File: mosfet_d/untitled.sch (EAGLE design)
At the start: 47 parts

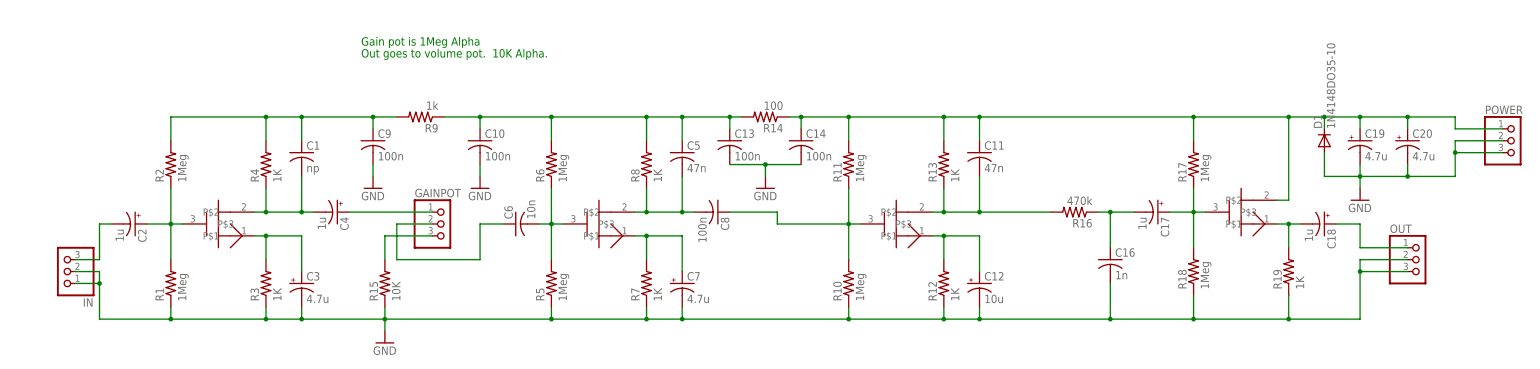
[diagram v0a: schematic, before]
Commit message: fixed pinout of transistors in mosfet d
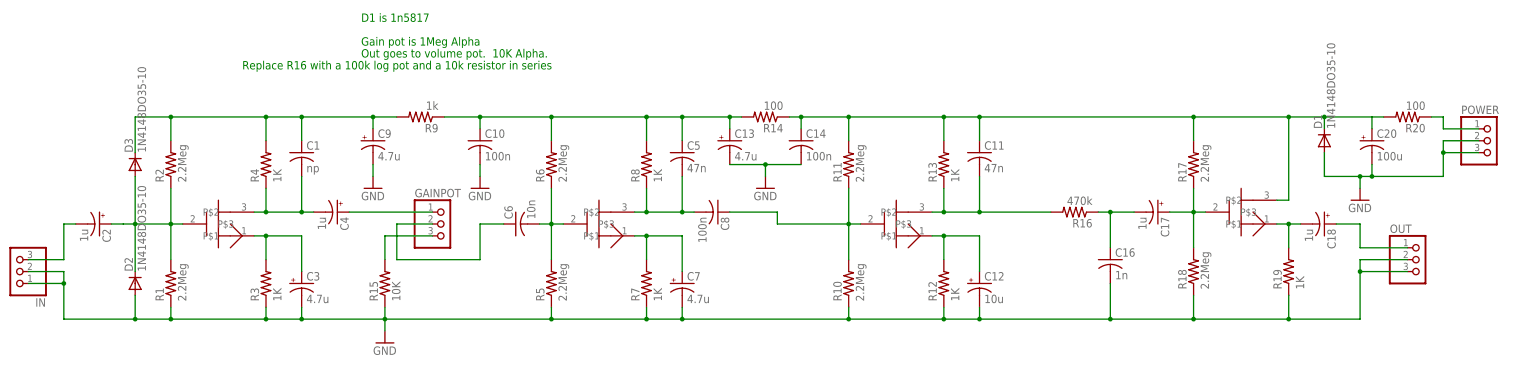
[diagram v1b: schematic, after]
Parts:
- removed C19: 4.7u, dan:CPOL-USE2-5
- added D2, D3: 1N4148DO35-10, dan:1N4148DO35-10
- added R20: 100, dan:R-US_0207/7
- C13, C9: value 100n -> 4.7u; device dan:C-US050-030X075 -> dan:CPOL-USE2-5
- C20: value 4.7u -> 100u
- R1, R10, R11, R17, R18, R2, R5, R6: value 1Meg -> 2.2Meg
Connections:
- new net N$17: C2.+
- new net N$18: POWER.1, R20.1
- net GND: now also C13.-, C9.-, D2.A; no longer C13.2, C19.-, C9.2
- net N$1: now also D2.C, D3.A; no longer C2.+
- net N$13: now also C13.+; no longer C13.1
- net N$20: now also R20.2; no longer C19.+, POWER.1
- net N$3: now also C9.+, D3.C; no longer C9.1
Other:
- note added: "D1 is 1n5817"
- note added: "Replace R16 with a 100k log pot and a 10k resistor in series"
- moved on the sheet: C2, C20, IN, POWER

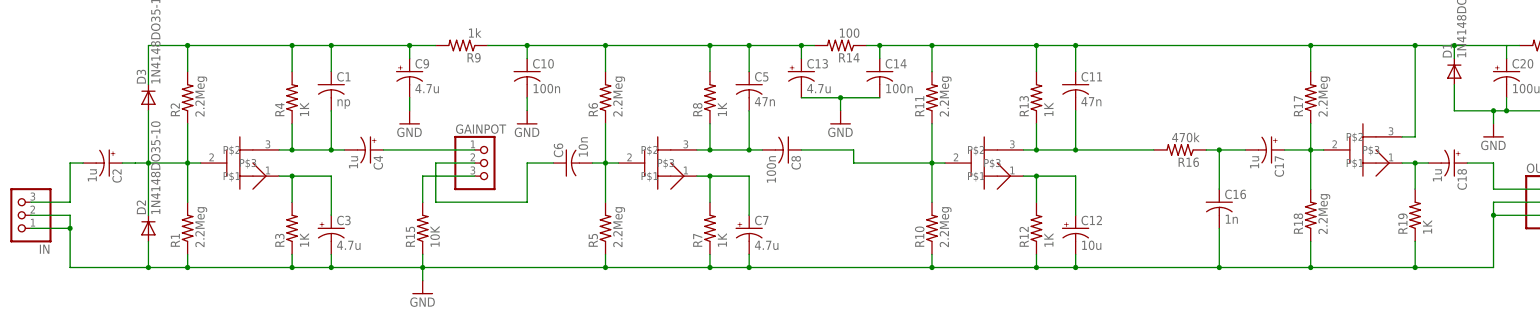
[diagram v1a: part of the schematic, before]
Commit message: fixed component values in mosfet d
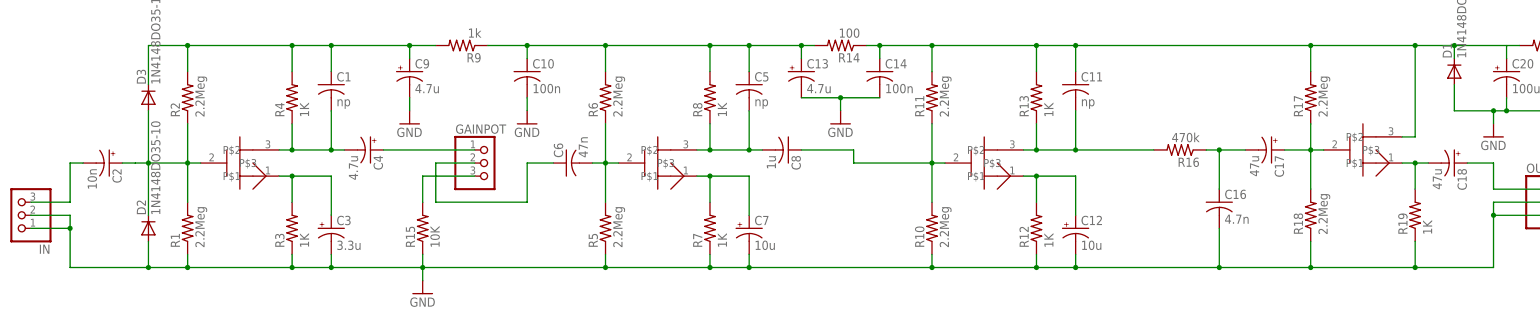
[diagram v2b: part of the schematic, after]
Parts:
- C11, C5: value 47n -> np
- C16: value 1n -> 4.7n
- C17, C18: value 1u -> 47u
- C2: value 1u -> 10n
- C3: value 4.7u -> 3.3u
- C4: value 1u -> 4.7u
- C6: value 10n -> 47n
- C7: value 4.7u -> 10u
- C8: value 100n -> 1u
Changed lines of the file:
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@@
 <part name="R3" library="dan" deviceset="R-US_" device="0207/7" value="1K"/>
 <part name="R4" library="dan" deviceset="R-US_" device="0207/7" value="1K"/>
-<part name="C2" library="dan" deviceset="CPOL-US" device="E2-5" value="1u"/>
-<part name="C3" library="dan" deviceset="CPOL-US" device="E2-5" value="4.7u"/>
+<part name="C2" library="dan" deviceset="CPOL-US" device="E2-5" value="10n"/>
+<part name="C3" library="dan" deviceset="CPOL-US" device="E2-5" value="3.3u"/>
 <part name="GAINPOT" library="dan" deviceset="PINHD-1X3" device=""/>
 <part name="GND1" library="dan" deviceset="GND" device=""/>
-<part name="C4" library="dan" deviceset="CPOL-US" device="E2-5" value="1u"/>
+<part name="C4" library="dan" deviceset="CPOL-US" device="E2-5" value="4.7u"/>
 <part name="U$2" library="dan" deviceset="2N7000_2" device=""/>
-<part name="C5" library="dan" deviceset="C-US" device="050-030X075" value="47n"/>
+<part name="C5" library="dan" deviceset="C-US" device="050-030X075" value="np"/>
 <part name="R5" library="dan" deviceset="R-US_" device="0207/7" value="2.2Meg"/>
 <part name="R6" library="dan" deviceset="R-US_" device="0207/7" value="2.2Meg"/>
 <part name="R7" library="dan" deviceset="R-US_" device="0207/7" value="1K"/>
 <part name="R8" library="dan" deviceset="R-US_" device="0207/7" value="1K"/>
-<part name="C7" library="dan" deviceset="CPOL-US" device="E2-5" value="4.7u"/>
-<part name="C6" library="dan" deviceset="C-US" device="050-030X075" value="10n"/>
-<part name="C8" library="dan" deviceset="C-US" device="050-030X075" value="100n"/>
+<part name="C7" library="dan" deviceset="CPOL-US" device="E2-5" value="10u"/>
+<part name="C6" library="dan" deviceset="C-US" device="050-030X075" value="47n"/>
+<part name="C8" library="dan" deviceset="C-US" device="050-030X075" value="1u"/>
 <part name="R9" library="dan" deviceset="R-US_" device="0207/7" value="1k"/>
 <part name="C10" library="dan" deviceset="C-US" device="050-030X075" value="100n"/>
@@
 <part name="GND3" library="dan" deviceset="GND" device=""/>
 <part name="U$3" library="dan" deviceset="2N7000_2" device=""/>
-<part name="C11" library="dan" deviceset="C-US" device="050-030X075" value="47n"/>
+<part name="C11" library="dan" deviceset="C-US" device="050-030X075" value="np"/>
 <part name="R10" library="dan" deviceset="R-US_" device="0207/7" value="2.2Meg"/>
 <part name="R11" library="dan" deviceset="R-US_" device="0207/7" value="2.2Meg"/>
@@
 <part name="GND4" library="dan" deviceset="GND" device=""/>
 <part name="R16" library="dan" deviceset="R-US_" device="0207/7" value="470k"/>
-<part name="C16" library="dan" deviceset="C-US" device="050-030X075" value="1n"/>
-<part name="C17" library="dan" deviceset="CPOL-US" device="E2-5" value="1u"/>
+<part name="C16" library="dan" deviceset="C-US" device="050-030X075" value="4.7n"/>
+<part name="C17" library="dan" deviceset="CPOL-US" device="E2-5" value="47u"/>
 <part name="R17" library="dan" deviceset="R-US_" device="0207/7" value="2.2Meg"/>
 <part name="R18" library="dan" deviceset="R-US_" device="0207/7" value="2.2Meg"/>
 <part name="U$4" library="dan" deviceset="2N7000_2" device=""/>
 <part name="R19" library="dan" deviceset="R-US_" device="0207/7" value="1K"/>
-<part name="C18" library="dan" deviceset="CPOL-US" device="E2-5" value="1u"/>
+<part name="C18" library="dan" deviceset="CPOL-US" device="E2-5" value="47u"/>
 <part name="OUT" library="dan" deviceset="PINHD-1X3" device=""/>
 <part name="IN" library="dan" deviceset="PINHD-1X3" device=""/>

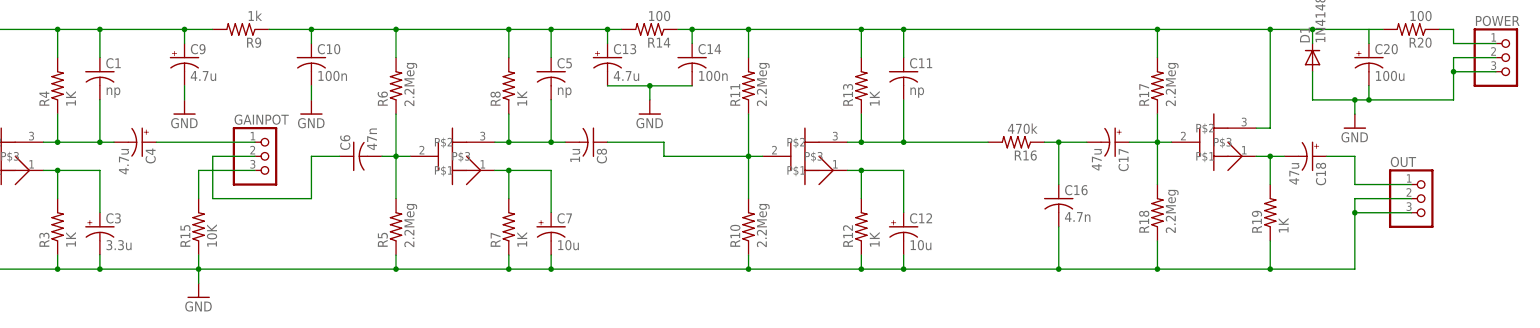
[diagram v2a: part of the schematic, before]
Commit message: added pcb mounted pots to distortion
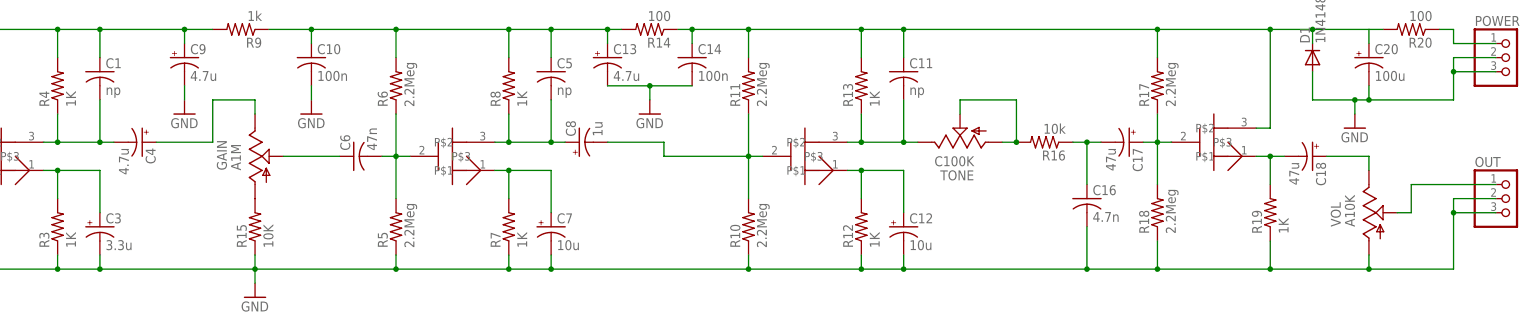
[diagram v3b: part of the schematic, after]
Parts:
- removed GAINPOT: (no value), dan:PINHD-1X3
- added GAIN: A1M, dan:PEDALPOT
- added TONE: C100K, dan:PEDALPOT
- added VOL: A10K, dan:PEDALPOT
- C8: device dan:C-US050-030X075 -> dan:CPOL-USE2-5
- R16: value 470k -> 10k
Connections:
- new net N$21: R16.2, TONE.A, TONE.S
- new net N$25: OUT.1, VOL.S
- net GND: now also VOL.A
- net N$11: now also GAIN.S; no longer GAINPOT.2
- net N$12: now also TONE.E; no longer R16.2
- net N$15: now also C8.-; no longer C8.1
- net N$16: now also GAIN.A; no longer GAINPOT.3
- net N$23: now also VOL.E; no longer OUT.1
- net N$4: now also GAIN.E; no longer GAINPOT.1
- net N$7: now also C8.+; no longer C8.2
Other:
- moved on the sheet: C16, C17, OUT, R15, R16

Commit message: redesigned the distortion pcb
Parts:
- added C15: np, dan:C-US050-030X075
- added C19: 10u, dan:CPOL-USE2-5
- added C21: 1u, dan:CPOL-USE2-5
- added C22: 22n, dan:C-US050-030X075
- added R21, R22: 2.2M, dan:R-US_0207/7
- added R23, R24: 1K, dan:R-US_0207/7
- added R25: 100k, dan:R-US_0207/7
- added R26: 22k, dan:R-US_0207/7
- added R27: 220k, dan:R-US_0207/7
- added U$5: 2N7000_2, dan:2N7000_2
- C12: value 10u -> 2.2u
- C2: device dan:CPOL-USE2-5 -> dan:C-US050-030X075
- C4: value 4.7u -> 22u
- C8: value 1u -> 4.7u
- R1, R10, R11, R17, R18, R2, R5, R6: value 2.2Meg -> 2.2M
- R16: value 10k -> short
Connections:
- removed net N$17: C2.+
- new net N$24: C15.2, R24.1, R25.2, U$5.P$2
- new net N$26: C19.+, R23.2, U$5.P$1
- new net N$27: C21.-, R21.2, R22.1, U$5.P$3
- new net N$28: C22.1, R26.2, R27.1
- new net N$29: R25.1, R26.1, TONE.E
- net GND: now also C19.-, C22.2, R21.1, R23.1, R27.2
- net N$1: now also C2.1
- net N$12: now also C21.+; no longer TONE.E
- net N$20: now also C15.1, R22.2, R24.2
- net N$8: now also C2.2; no longer C2.-
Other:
- note removed: "Gain pot is 1Meg Alpha"
- note removed: "Out goes to volume pot. 10K Alpha."
- note removed: "Replace R16 with a 100k log pot and a 10k resistor in series"
- moved on the sheet: C16, C17, C18, C20, D1, OUT, POWER, R16, R17, R18, R19, R20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
